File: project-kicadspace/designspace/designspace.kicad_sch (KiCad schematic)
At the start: 39 parts, among them J1 PJ-313B, U3 MAX9812

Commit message: feat(pcb): import pin socket for voltage divider source 12->12/5/3.3, prepared for final validation to pcb manufacturing
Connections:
- net 3.3V: no longer ESP32.3V3.
- net 5V: no longer ESP32.5V0
- net 9V renamed 12V
- no-connect marks 39 -> 46
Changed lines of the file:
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@@
 	)
 	(no_connect
+		(at 167.64 66.04)
+	)
+	(no_connect
 		(at 38.1 119.38)
 	)
 	(no_connect
+		(at 88.9 78.74)
+	)
+	(no_connect
 		(at 83.82 132.08)
 	)
@@
 	)
 	(no_connect
+		(at 83.82 137.16)
+	)
+	(no_connect
 		(at 83.82 116.84)
 	)
@@
 	)
 	(no_connect
+		(at 93.98 125.73)
+	)
+	(no_connect
 		(at 163.83 40.64)
 	)
@@
 	)
 	(no_connect
+		(at 175.26 22.86)
+	)
+	(no_connect
+		(at 77.47 63.5)
+	)
+	(no_connect
 		(at 83.82 129.54)
 	)
@@
 	)
 	(no_connect
+		(at 83.82 88.9)
+	)
+	(no_connect
 		(at 38.1 101.6)
 	)
@@
 	)
 	(symbol
-		(lib_id "power:VCC")
-		(at 83.82 137.16 270)
-		(mirror x)
-		(unit 1)
-		(exclude_from_sim no)
-		(in_bom yes)
-		(on_board yes)
-		(dnp no)
-		(property "Reference" "#PWR04"
-			(at 80.01 137.16 0)
-			(effects
-				(font
-					(size 1.27 1.27)
-				)
-				(hide yes)
-			)
-		)
-		(property "Value" "5V"
-			(at 88.646 137.16 0)
-			(effects
-				(font
-					(size 1.27 1.27)
-				)
-			)
-		)
-		(property "Footprint" ""
-			(at 83.82 137.16 0)
-			(effects
-				(font
-					(size 1.27 1.27)
-				)
-				(hide yes)
-			)
-		)
-		(property "Datasheet" ""
-			(at 83.82 137.16 0)
-			(effects
-				(font
-					(size 1.27 1.27)
-				)
-				(hide yes)
-			)
-		)
-		(property "Description" "Power symbol creates a global label with name \"VCC\""
-			(at 83.82 137.16 0)
-			(effects
-				(font
-					(size 1.27 1.27)
-				)
-				(hide yes)
-			)
-		)
-		(pin "1"
-		)
-		(instances
-			(project "designspace"
-				(path "/bc3d2117-c577-44c7-883b-e059e61f0c28"
-					(reference "#PWR04")
-					(unit 1)
-				)
-			)
-		)
-	)
-	(symbol
 		(lib_id "Device:Microphone_Ultrasound")
 		(at 214.63 125.73 270)
@@
 	)
 	(symbol
+		(lib_id "power:VCC")
+		(at 233.68 49.53 0)
+		(mirror y)
+		(unit 1)
+		(exclude_from_sim no)
+		(in_bom yes)
+		(on_board yes)
+		(dnp no)
+		(property "Reference" "#PWR022"
+			(at 233.68 53.34 0)
+			(effects
+				(font
+					(size 1.27 1.27)
+				)
+				(hide yes)
+			)
+		)
+		(property "Value" "12V"
+			(at 233.68 44.704 0)
+			(effects
+				(font
+					(size 1.27 1.27)
+				)
+			)
+		)
+		(property "Footprint" ""
+			(at 233.68 49.53 0)
+			(effects
+				(font
+					(size 1.27 1.27)
+				)
+				(hide yes)
+			)
+		)
+		(property "Datasheet" ""
+			(at 233.68 49.53 0)
+			(effects
+				(font
+					(size 1.27 1.27)
+				)
+				(hide yes)
+			)
+		)
+		(property "Description" "Power symbol creates a global label with name \"VCC\""
+			(at 233.68 49.53 0)
+			(effects
+				(font
+					(size 1.27 1.27)
+				)
+				(hide yes)
+			)
+		)
+		(pin "1"
+		)
+		(instances
+			(project "designspace"
+				(path "/bc3d2117-c577-44c7-883b-e059e61f0c28"
+					(reference "#PWR022")
+					(unit 1)
+				)
+			)
+		)
+	)
+	(symbol
 		(lib_id "74xx:74HC04")
 		(at 138.43 40.64 0)
@@
 	)
 	(symbol
-		(lib_id "power:VCC")
-		(at 233.68 49.53 0)
-		(mirror y)
-		(unit 1)
-		(exclude_from_sim no)
-		(in_bom yes)
-		(on_board yes)
-		(dnp no)
-		(property "Reference" "#PWR036"
-			(at 233.68 53.34 0)
-			(effects
-				(font
-					(size 1.27 1.27)
-				)
-				(hide yes)
-			)
-		)
-		(property "Value" "9V"
-			(at 230.886 49.53 0)
-			(effects
-				(font
-					(size 1.27 1.27)
-				)
-			)
-		)
-		(property "Footprint" ""
-			(at 233.68 49.53 0)
-			(effects
-				(font
-					(size 1.27 1.27)
-				)
-				(hide yes)
-			)
-		)
-		(property "Datasheet" ""
-			(at 233.68 49.53 0)
-			(effects
-				(font
-					(size 1.27 1.27)
-				)
-				(hide yes)
-			)
-		)
-		(property "Description" "Power symbol creates a global label with name \"VCC\""
-			(at 233.68 49.53 0)
-			(effects
-				(font
-					(size 1.27 1.27)
-				)
-				(hide yes)
-			)
-		)
-		(pin "1"
-		)
-		(instances
-			(project "designspace"
-				(path "/bc3d2117-c577-44c7-883b-e059e61f0c28"
-					(reference "#PWR036")
-					(unit 1)
-				)
-			)
-		)
-	)
-	(symbol
 		(lib_id "Device:C")
 		(at 96.52 59.69 0)
@@
 		(on_board yes)
 		(dnp no)
-		(fields_autoplaced yes)
 		(property "Reference" "#FLG05"
 			(at 43.18 55.245 0)
@@
 			)
 		)
-		(property "Value" "9V"
-			(at 43.18 52.07 0)
+		(property "Value" "12V"
+			(at 41.656 52.07 0)
 			(effects
 				(font
 					(size 1.27 1.27)
 				)
+				(justify left)
 			)
 		)
@@
 	(symbol
 		(lib_id "power:VCC")
-		(at 83.82 88.9 270)
-		(mirror x)
-		(unit 1)
-		(exclude_from_sim no)
-		(in_bom yes)
-		(on_board yes)
-		(dnp no)
-		(fields_autoplaced yes)
-		(property "Reference" "#PWR05"
-			(at 80.01 88.9 0)
-			(effects
-				(font
-					(size 1.27 1.27)
-				)
-				(hide yes)
-			)
-		)
-		(property "Value" "3.3V"
-			(at 87.63 88.8999 90)
-			(effects
-				(font
-					(size 1.27 1.27)
-				)
-				(justify left)
-			)
-		)
-		(property "Footprint" ""
-			(at 83.82 88.9 0)
-			(effects
-				(font
-					(size 1.27 1.27)
-				)
-				(hide yes)
-			)
-		)
-		(property "Datasheet" ""
-			(at 83.82 88.9 0)
-			(effects
-				(font
-					(size 1.27 1.27)
-				)
-				(hide yes)
-			)
-		)
-		(property "Description" "Power symbol creates a global label with name \"VCC\""
-			(at 83.82 88.9 0)
-			(effects
-				(font
-					(size 1.27 1.27)
-				)
-				(hide yes)
-			)
-		)
-		(pin "1"
-		)
-		(instances
-			(project "designspace"
-				(path "/bc3d2117-c577-44c7-883b-e059e61f0c28"
-					(reference "#PWR05")
-					(unit 1)
-				)
-			)
-		)
-	)
-	(symbol
-		(lib_id "power:VCC")
 		(at 31.75 34.29 90)
 		(mirror x)
@@
 			)
 		)
-		(property "Value" "9V"
+		(property "Value" "12V"
 			(at 43.18 61.976 0)
 			(effects

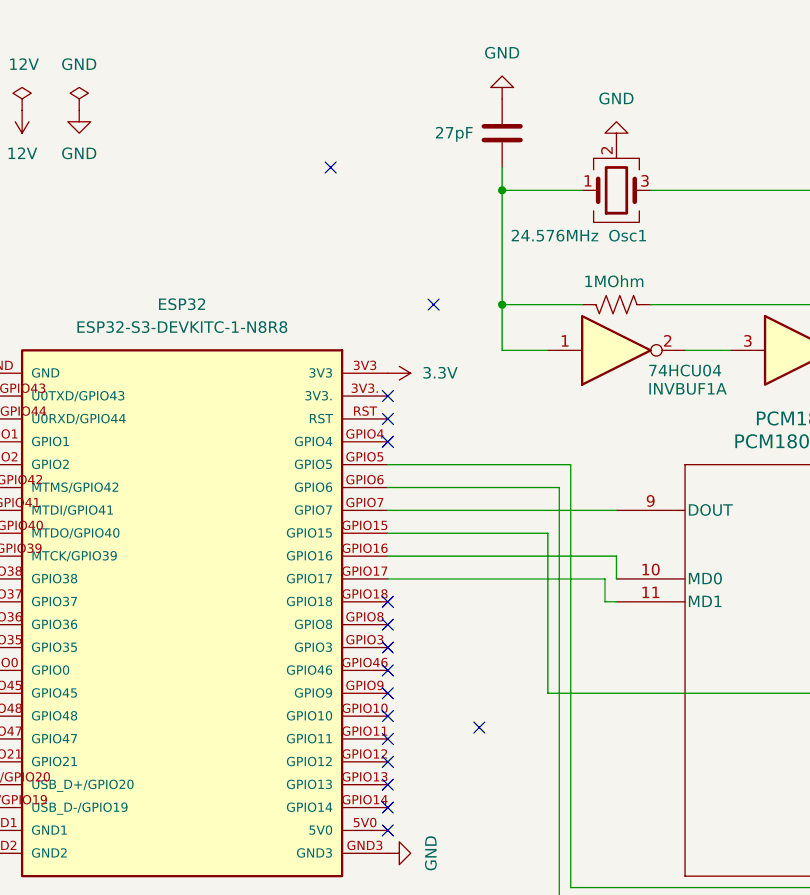
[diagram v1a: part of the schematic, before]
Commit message: feat(pcb): add round corner & adjust size for actual components
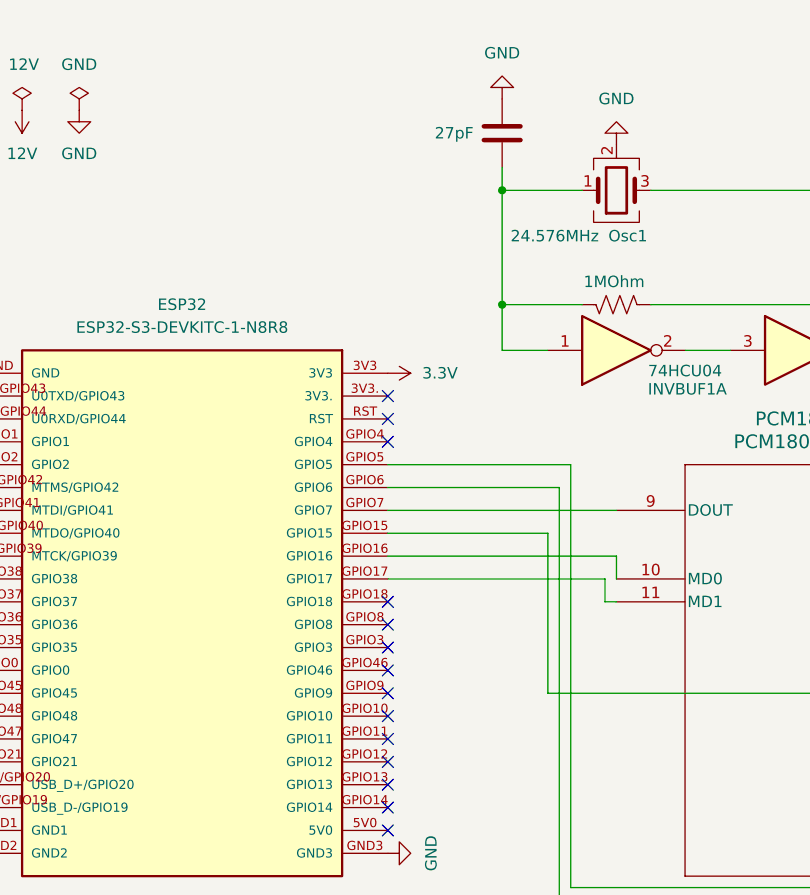
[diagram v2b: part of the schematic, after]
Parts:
- INVBUF1: footprint (none) -> Package_SO:SO-14_3.9x8.65mm_P1.27mm
- INVBUF1: footprint Package_SO:SO-14_5.3x10.2mm_P1.27mm -> Package_SO:SO-14_3.9x8.65mm_P1.27mm
- Osc1: footprint Crystal:Crystal_SMD_7050-4Pin_7.0x5.0mm -> Crystal:Crystal_SMD_3225-4Pin_3.2x2.5mm_HandSoldering
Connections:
- no-connect marks 46 -> 43
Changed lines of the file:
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@@
 	)
 	(no_connect
-		(at 88.9 78.74)
-	)
-	(no_connect
 		(at 83.82 132.08)
 	)
@@
 	)
 	(no_connect
-		(at 93.98 125.73)
-	)
-	(no_connect
 		(at 163.83 40.64)
 	)
@@
 	)
 	(no_connect
-		(at 77.47 63.5)
-	)
-	(no_connect
 		(at 83.82 129.54)
 	)
@@
 			)
 		)
-		(property "Footprint" ""
+		(property "Footprint" "Package_SO:SO-14_3.9x8.65mm_P1.27mm"
 			(at 101.6 40.64 0)
 			(effects
@@
 			)
 		)
-		(property "Footprint" ""
+		(property "Footprint" "Package_SO:SO-14_3.9x8.65mm_P1.27mm"
 			(at 156.21 40.64 0)
 			(effects
@@
 			)
 		)
-		(property "Footprint" ""
+		(property "Footprint" "Package_SO:SO-14_3.9x8.65mm_P1.27mm"
 			(at 138.43 40.64 0)
 			(effects
@@
 			)
 		)
-		(property "Footprint" ""
+		(property "Footprint" "Package_SO:SO-14_3.9x8.65mm_P1.27mm"
 			(at 129.54 83.82 0)
 			(effects
@@
 			)
 		)
-		(property "Footprint" ""
+		(property "Footprint" "Package_SO:SO-14_3.9x8.65mm_P1.27mm"
 			(at 120.65 40.64 0)
 			(effects
@@
 			)
 		)
-		(property "Footprint" "Crystal:Crystal_SMD_7050-4Pin_7.0x5.0mm"
+		(property "Footprint" "Crystal:Crystal_SMD_3225-4Pin_3.2x2.5mm_HandSoldering"
 			(at 109.22 66.04 0)
 			(effects
@@
 			)
 		)
-		(property "Footprint" "Package_SO:SO-14_5.3x10.2mm_P1.27mm"
+		(property "Footprint" "Package_SO:SO-14_3.9x8.65mm_P1.27mm"
 			(at 44.45 34.29 0)
 			(effects
@@
 			)
 		)
-		(property "Footprint" "Package_SO:SO-14_5.3x10.2mm_P1.27mm"
+		(property "Footprint" "Package_SO:SO-14_3.9x8.65mm_P1.27mm"
 			(at 109.22 83.82 0)
 			(effects
